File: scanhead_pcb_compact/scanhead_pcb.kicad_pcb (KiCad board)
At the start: 2 copper layers, 35.1 x 32.8 mm, 21 parts, among them J2 FPC 15 pin molex vertical, J3 FPC molex 4 pin, J6 jumper wire 2 pin, J7 jumper wire 2 pin, Q1 IRFML8244, U1 DIGIPOT_50K, U2 U_IC-HKB, U3 STSPIN230

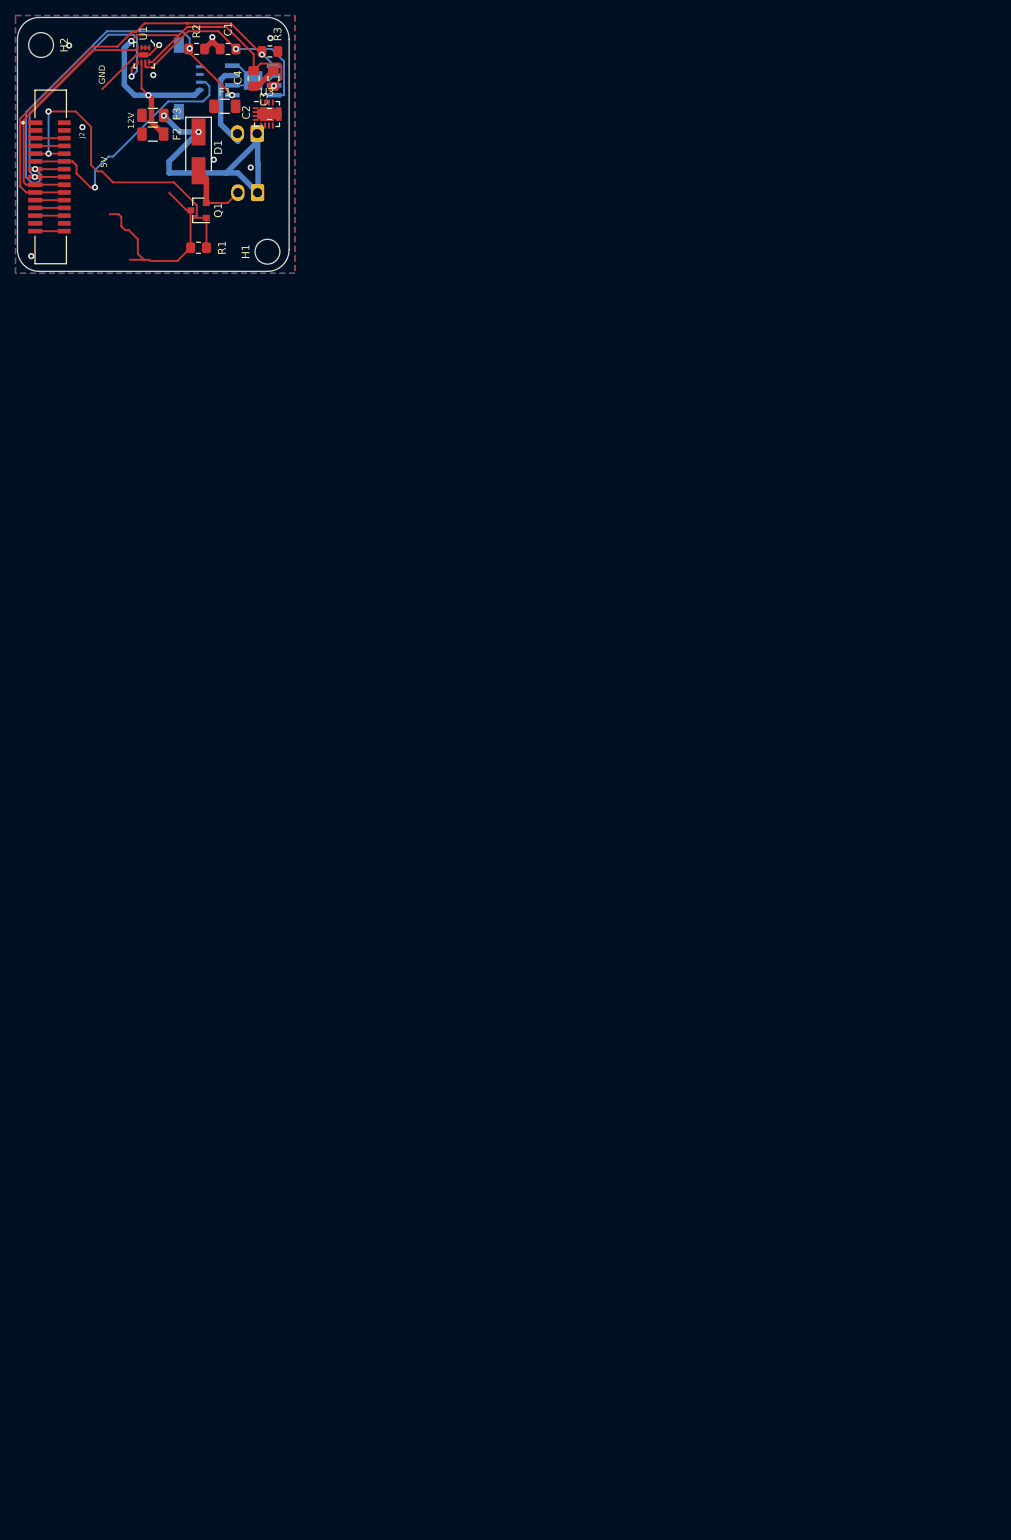
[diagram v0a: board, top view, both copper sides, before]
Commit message: updated compact scanhead
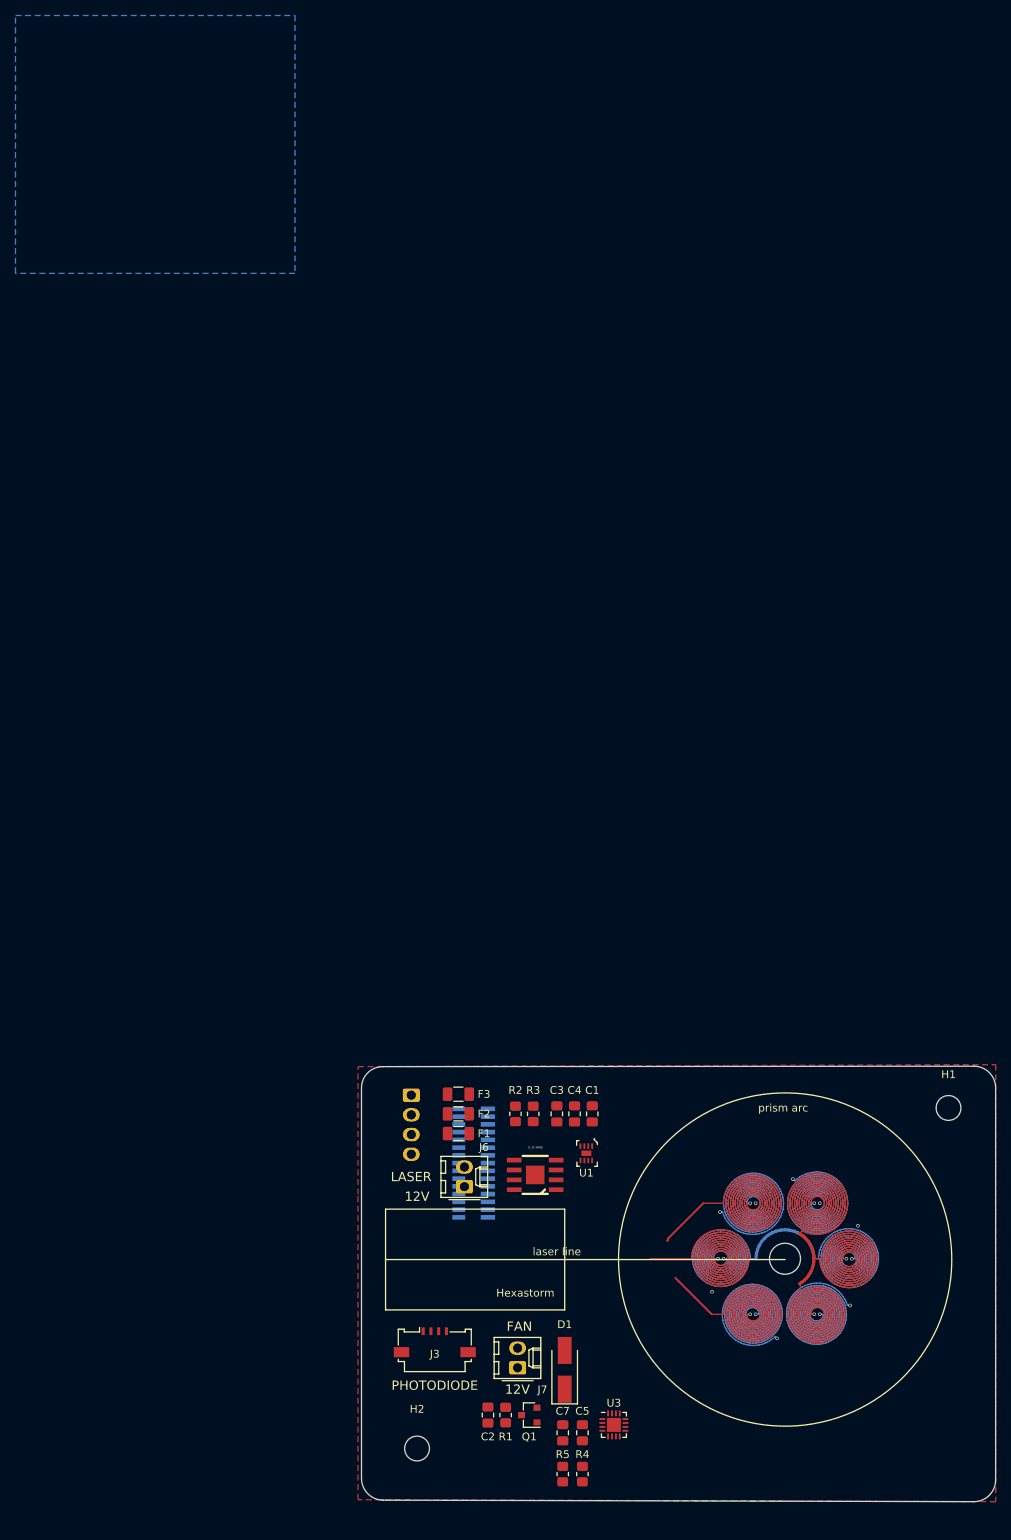
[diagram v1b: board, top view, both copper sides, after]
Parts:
- added C5: 10nF, Capacitor_SMD:C_0805_2012Metric_Pad1.18x1.45mm_HandSolder, F.Cu at (106.7, 130.8)
- added C7: 100nF, Capacitor_SMD:C_0805_2012Metric_Pad1.18x1.45mm_HandSolder, F.Cu at (104.1, 130.8)
- added J1: Screw_Terminal_01x04, Connector_Molex:Molex_KK-254_AE-6410-04A_1x04_P2.54mm_Vertical, B.Cu at (84.6, 87.2)
- added R4: 10K, Resistor_SMD:R_0805_2012Metric_Pad1.20x1.40mm_HandSolder, F.Cu at (106.7, 136.1)
- added R5: 10K, Resistor_SMD:R_0805_2012Metric_Pad1.20x1.40mm_HandSolder, F.Cu at (104.1, 136.1)
- C1, C2, C3, C4: footprint Capacitor_SMD:C_0805_2012Metric_Pad1.15x1.40mm_HandSolder -> Capacitor_SMD:C_0805_2012Metric_Pad1.18x1.45mm_HandSolder
- J2: moved to B.Cu
- J3, J6, J7, U2: moved to F.Cu
- R1, R2, R3: footprint Resistor_SMD:R_0805_2012Metric_Pad1.15x1.40mm_HandSolder -> Resistor_SMD:R_0805_2012Metric_Pad1.20x1.40mm_HandSolder
- moved H2 187.5 mm to (85.3, 132.8)
- moved U3 175.0 mm to (110.7, 129.8)
- moved C2 170.2 mm to (94.5, 128.5), turned to -90 degrees
- moved J3 165.6 mm to (87.6, 118.6), turned to 0 degrees
- moved D1 164.2 mm to (104.4, 122.7), turned to 90 degrees
- moved Q1 161.2 mm to (99.8, 128.5)
- moved R1 155.7 mm to (96.8, 128.5), turned to 90 degrees
- moved J7 155.3 mm to (98.3, 122.4), turned to 90 degrees
- moved U1 152.8 mm to (107.2, 94.7)
- moved U2 145.8 mm to (100.6, 97.5)
- moved C1 145.2 mm to (108.0, 89.7), turned to 90 degrees
- moved R2 143.4 mm to (98.0, 89.7), turned to 90 degrees
- moved R3 141.2 mm to (100.3, 89.7), turned to -90 degrees
- moved H1 141.2 mm to (153.9, 88.9)
- moved C4 139.9 mm to (105.7, 89.7)
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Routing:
- net PH1: track 0.00 -> 3858.0 mm, vias 0 -> 18
- net +5V: track 59.6 -> 0.00 mm, vias 3 -> 0
- net IC_HB_PWM1: track 55.2 -> 0.00 mm, vias 1 -> 0
- net GND: track 52.8 -> 0.00 mm, vias 9 -> 0
- net IC_HB_PWM2: track 51.5 -> 0.00 mm, vias 3 -> 0
- net FAN_PWM: track 43.6 -> 0.00 mm, vias 2 -> 0
- net POT_SCL: track 37.9 -> 0.00 mm, vias 2 -> 0
- net +12V: track 37.0 -> 0.00 mm, vias 2 -> 0
- net DIGITAL1: track 33.3 -> 0.00 mm, vias 1 -> 0
- net POT_SDA: track 32.0 -> 0.00 mm
- net POT_W: track 27.7 -> 0.00 mm, vias 1 -> 0
- net LDK: track 10.6 -> 0.00 mm
- net Net-(D1-Pad2): track 9.22 -> 0.00 mm
- net +3V3: track 3.76 -> 0.00 mm
- net PWM3L: track 3.75 -> 0.00 mm
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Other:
- board size 35.1 x 32.8 mm -> 81.8 x 56.2 mm
- copper layers 2 -> 4
- rule pad_to_mask_clearance: 0.051 -> 0
- board text added: "10V"
- board text added: "PHOTODIODE"
- board text added: "laser line"
- board text added: "prism arc"
- board text removed: "PHOTODIODE ANALOG"
- board text removed: "PHOTODIODE DIGITAL"
- board text removed: "POLYGON"

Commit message: updated model
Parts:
- removed H1, H2: MountingHole, MountingHole:MountingHole_3.2mm_M3
- moved J1 81.9 mm to (151.1, 135.1), turned to 90 degrees
- moved F3 72.0 mm to (144.8, 134.6), turned to 0 degrees
- moved F2 68.7 mm to (144.8, 132.1), turned to 180 degrees
- moved F1 65.7 mm to (144.8, 129.5), turned to 180 degrees
- moved J3 62.2 mm to (148.1, 103.9), turned to 180 degrees
- moved J2 61.0 mm to (145.3, 126.5), turned to 90 degrees
- moved R2 59.5 mm to (138.9, 132.8), turned to -90 degrees
- moved C2 59.3 mm to (142.5, 93.7), turned to 90 degrees
- moved J6 58.2 mm to (144.3, 123.4), turned to -90 degrees
- moved R3 56.4 mm to (136.7, 132.8), turned to 90 degrees
- moved R1 55.7 mm to (140.2, 93.7), turned to -90 degrees
- moved C3 53.1 mm to (134.4, 132.8), turned to 90 degrees
- moved Q1 51.0 mm to (137.2, 93.7), turned to 0 degrees
- moved C4 50.6 mm to (132.1, 132.8), turned to -90 degrees
- moved C1 48.4 mm to (129.8, 132.8), turned to -90 degrees
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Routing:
- net +12V: track 0.00 -> 666.4 mm
- net PH1: track 3858.0 -> 3191.6 mm
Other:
- board size 81.8 x 56.2 mm -> 81.2 x 59.1 mm

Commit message: updated boards
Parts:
- removed D1: 50V_1A, Diode_SMD:D_SMA_Handsoldering
- removed J7: jumper wire 2 pin, Connector_Molex:Molex_KK-254_AE-6410-02A_1x02_P2.54mm_Vertical
- removed Q1: IRFML8244, Package_TO_SOT_SMD:SOT-23
- added C6: 220pF, Capacitor_SMD:C_0805_2012Metric_Pad1.18x1.45mm_HandSolder, F.Cu at (139.4, 103.9)
- added C8: 1uF, Capacitor_SMD:C_0805_2012Metric_Pad1.18x1.45mm_HandSolder, F.Cu at (139.4, 106.2)
- added R10: 22K, Resistor_SMD:R_0805_2012Metric_Pad1.20x1.40mm_HandSolder, F.Cu at (146.8, 103.6)
- added R11: 1K5, Resistor_SMD:R_0805_2012Metric_Pad1.20x1.40mm_HandSolder, F.Cu at (146.8, 105.7)
- added R12: 8K2, Resistor_SMD:R_0805_2012Metric_Pad1.20x1.40mm_HandSolder, F.Cu at (139.4, 99.3)
- added R6: 8K2, Resistor_SMD:R_0805_2012Metric_Pad1.20x1.40mm_HandSolder, F.Cu at (146.8, 94.7)
- added R7: 22K, Resistor_SMD:R_0805_2012Metric_Pad1.20x1.40mm_HandSolder, F.Cu at (146.8, 96.8)
- added R8: 8K2, Resistor_SMD:R_0805_2012Metric_Pad1.20x1.40mm_HandSolder, F.Cu at (146.8, 98.8)
- added R9: 8K2, Resistor_SMD:R_0805_2012Metric_Pad1.20x1.40mm_HandSolder, F.Cu at (146.8, 101.6)
- added TP2: HSync, TestPoint:TestPoint_Pad_D1.0mm, F.Cu at (152.4, 98.8)
- added U4: MIC920, Package_TO_SOT_SMD:SOT-353_SC-70-5_Handsoldering, F.Cu at (140.0, 93.5)
- added U5: MIC920, Package_TO_SOT_SMD:SOT-353_SC-70-5_Handsoldering, F.Cu at (140.0, 96.5)
- J3: value FPC molex 4 pin -> Conn_01x02; footprint sockets_scanhead:Molex_200528-0040_1x04-1MP_P1.00mm_Horizontal -> Connector_PinHeader_2.54mm:PinHeader_1x02_P2.54mm_Vertical
- R1: value 10K -> 22K
- moved U3 40.5 mm to (124.7, 133.1)
- moved J3 21.4 mm to (129.5, 93.2), turned to 0 degrees
- moved C2 14.5 mm to (130.3, 101.6)
- moved J2 13.2 mm to (132.1, 126.0)
- moved C7 10.6 mm to (128.0, 101.6)
- moved C5 10.5 mm to (126.0, 101.6)
- moved R1 7.91 mm to (139.4, 101.6), turned to 0 degrees
- moved R5 7.62 mm to (128.0, 107.4)
- moved R4 7.62 mm to (130.0, 107.4)
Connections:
- J3 pad 1: +5V -> GND
- J3 pad 2: DIGITAL1 -> Net-(C6-Pad2)
- R1 pad 1: FAN_PWM -> Net-(R1-Pad1)
- R1 pad 2: GND -> +5V
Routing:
- net +3V3: track 0.00 -> 166.8 mm
- net PH1: track 3191.6 -> 3024.8 mm
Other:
- board size 81.2 x 59.1 mm -> 81.2 x 56 mm
- board text removed: "FAN"
- board text removed: "PHOTODIODE"

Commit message: routed new boards for compact scanhead
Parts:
- added C9: 10nF, Capacitor_SMD:C_0805_2012Metric_Pad1.18x1.45mm_HandSolder, F.Cu at (143.4, 104.6)
- added R13: 10K, Resistor_SMD:R_0805_2012Metric_Pad1.20x1.40mm_HandSolder, B.Cu at (117.9, 102.6)
- added R14: 10K, Resistor_SMD:R_0805_2012Metric_Pad1.20x1.40mm_HandSolder, B.Cu at (93.5, 102.5)
- added R15: 10K, Resistor_SMD:R_0805_2012Metric_Pad1.20x1.40mm_HandSolder, B.Cu at (104.9, 130.0)
- added U6: DRV5033FAxDBZ, Package_TO_SOT_SMD:SOT-23, B.Cu at (116.0, 107.5)
- added U7: DRV5033FAxDBZ, Package_TO_SOT_SMD:SOT-23, B.Cu at (94.0, 107.9)
- added U8: DRV5033FAxDBZ, Package_TO_SOT_SMD:SOT-23, B.Cu at (104.9, 126.8)
- moved C7 37.8 mm to (112.2, 136.0), turned to 180 degrees
- moved C5 35.1 mm to (117.2, 135.5)
- moved R5 30.9 mm to (115.1, 135.5), turned to -90 degrees
- moved C2 30.5 mm to (152.1, 122.9), turned to 180 degrees
- moved R4 30.0 mm to (119.4, 135.5)
- moved J2 21.7 mm to (150.4, 114.4)
- moved R9 9.40 mm to (143.2, 92.9)
- moved R6 9.22 mm to (139.1, 99.8), turned to 180 degrees
- moved R1 8.62 mm to (139.0, 93.0)
- moved R12 8.02 mm to (147.5, 99.8), turned to 180 degrees
- moved J1 7.12 mm to (151.1, 128.0), turned to -90 degrees
- moved R8 5.87 mm to (147.2, 92.9)
- moved F1 5.67 mm to (145.7, 135.1)
- moved U5 5.10 mm to (145.1, 96.3)
- moved R10 4.92 mm to (151.6, 102.3)
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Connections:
- J2 pad 1: unconnected-(J2-Pad1) -> PWM2L
- J2 pad 10: IC_HB_PWM1 -> PWM3H
- J2 pad 10_1: IC_HB_PWM1 -> PWM3H
- J2 pad 11: PWM2L -> HALL1
- J2 pad 11_1: PWM2L -> HALL1
- J2 pad 12: PWM2H -> HALL2
- J2 pad 12_1: PWM2H -> HALL2
- J2 pad 13: PWM3L -> HALL3
- J2 pad 13_1: PWM3L -> HALL3
- J2 pad 14: PWM3H -> DIGITAL
- J2 pad 14_1: PWM3H -> DIGITAL
- J2 pad 1_1: unconnected-(J2-Pad1_1) -> PWM2L
- J2 pad 2: unconnected-(J2-Pad2) -> PWM2H
- J2 pad 2_1: unconnected-(J2-Pad2_1) -> PWM2H
- J2 pad 5: FAN_PWM -> POT_SDA
- J2 pad 5_1: FAN_PWM -> POT_SDA
- J2 pad 6: DIGITAL1 -> POT_SCL
- J2 pad 6_1: DIGITAL1 -> POT_SCL
- J2 pad 7: IC_HB_PWM2 -> IC_HB_PWM1
- J2 pad 7_1: IC_HB_PWM2 -> IC_HB_PWM1
- J2 pad 8: POT_SCL -> IC_HB_PWM2
- J2 pad 8_1: POT_SCL -> IC_HB_PWM2
- J2 pad 9: POT_SDA -> PWM3L
- J2 pad 9_1: POT_SDA -> PWM3L
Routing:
- net PH1: track 3024.8 -> 3924.9 mm
- net +12V: track 666.4 -> 15.0 mm
- net +5V: track 0.00 -> 152.6 mm
- net GND: track 0.00 -> 136.1 mm, vias 0 -> 18
- net HALL3: track 0.00 -> 74.1 mm
- net HALL1: track 0.00 -> 59.3 mm
- net PWM3H: track 0.00 -> 44.3 mm, vias 0 -> 1
- net HALL2: track 0.00 -> 43.2 mm, vias 0 -> 2
- net +10V: track 0.00 -> 42.2 mm, vias 0 -> 3
- net PWM3L: track 0.00 -> 41.4 mm, vias 0 -> 1
- net +3V3: track 166.8 -> 127.1 mm, vias 0 -> 4
- net IC_HB_PWM2: track 0.00 -> 39.2 mm, vias 0 -> 1
- net PWM2L: track 0.00 -> 39.0 mm, vias 0 -> 1
- net IC_HB_PWM1: track 0.00 -> 38.8 mm, vias 0 -> 1
- net PWM2H: track 0.00 -> 37.9 mm, vias 0 -> 1
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- added copper zone on In1.Cu, net GND
- added copper zone on In2.Cu, net GND

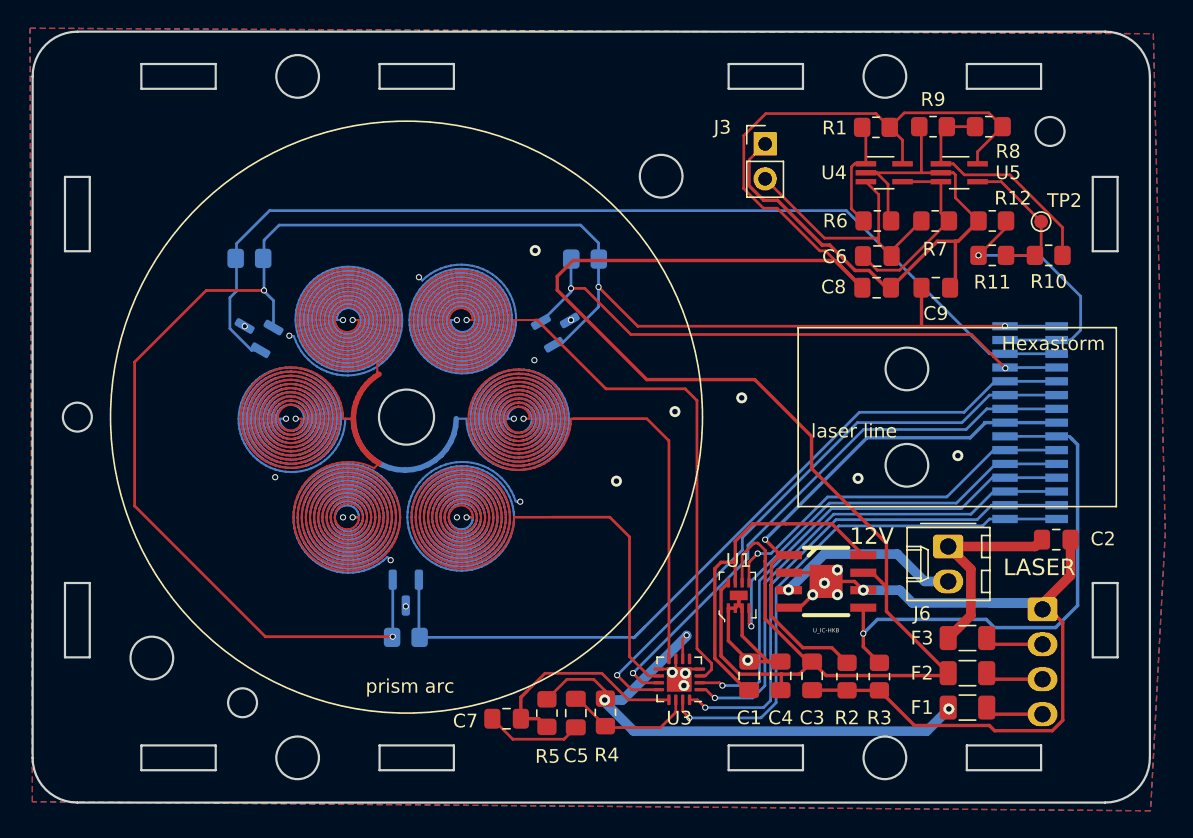
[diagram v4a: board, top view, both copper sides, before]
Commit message: added two holes, rerouted board
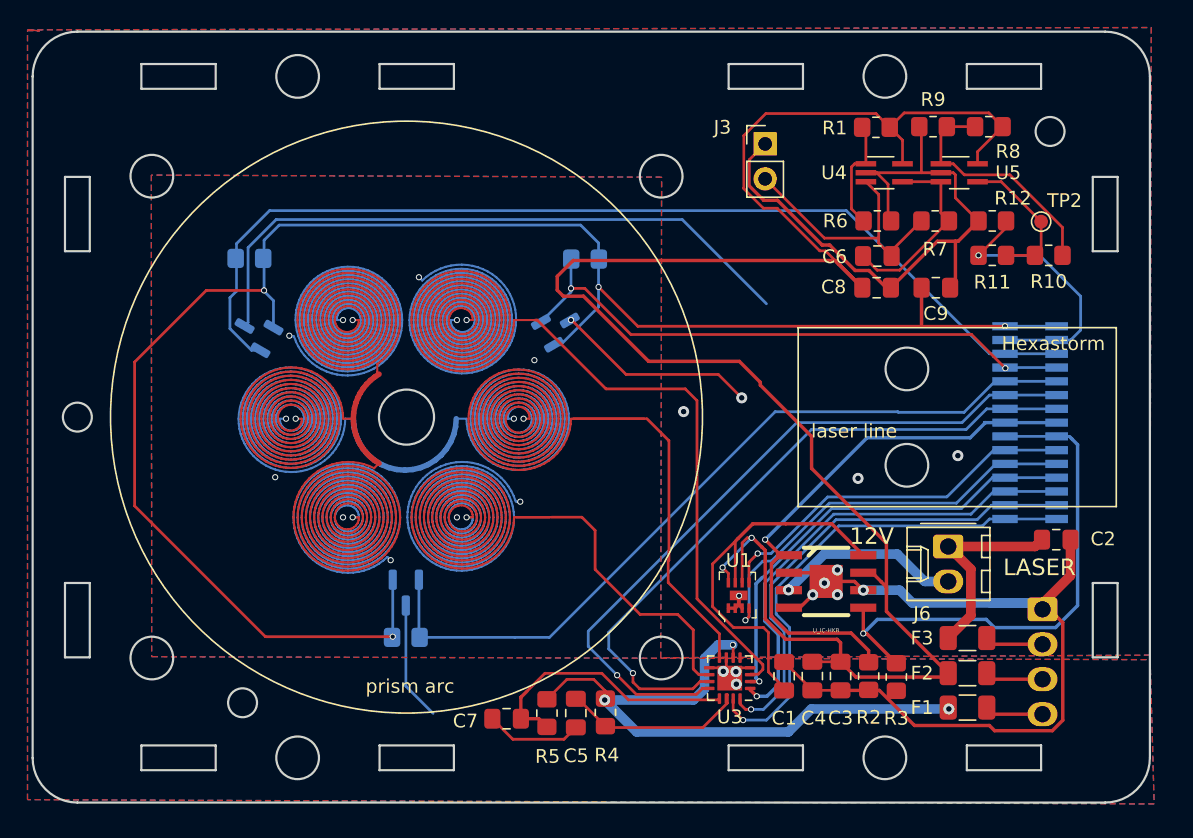
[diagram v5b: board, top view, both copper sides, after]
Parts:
- moved U3 3.67 mm to (128.4, 133.0)
- moved C1 2.54 mm to (132.3, 132.9)
- moved C4 2.30 mm to (134.4, 132.9), turned to 90 degrees
- moved C3 2.07 mm to (136.4, 132.9)
- moved R2 1.57 mm to (138.5, 132.9)
- moved R3 1.23 mm to (140.5, 132.9)
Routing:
- net GND: track 136.1 -> 194.6 mm, vias 18 -> 14
- net PWM3H: track 44.3 -> 52.6 mm
- net PWM3L: track 41.4 -> 49.6 mm
- net +5V: track 152.6 -> 146.6 mm, vias 0 -> 2
- net PH1: track 3924.9 -> 3929.8 mm
- net Net-(C5-Pad1): track 9.49 -> 13.5 mm
- net Net-(C7-Pad1): track 16.0 -> 19.7 mm
- net POT_W: track 25.5 -> 29.0 mm
- net +10V: track 42.2 -> 45.6 mm
- net PWM1H: track 36.6 -> 33.2 mm
- net PWM2H: track 37.9 -> 35.5 mm
- net PWM1L: track 36.8 -> 34.4 mm
- net PWM2L: track 39.0 -> 36.7 mm
- net IC_HB_PWM2: track 39.2 -> 41.2 mm
- net HALL1: track 59.3 -> 58.2 mm
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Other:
- outline, holes or cut-outs redrawn
